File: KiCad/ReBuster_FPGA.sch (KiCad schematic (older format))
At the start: 30 parts, among them U1 10M02SCU169, U2 LM1117-3.3

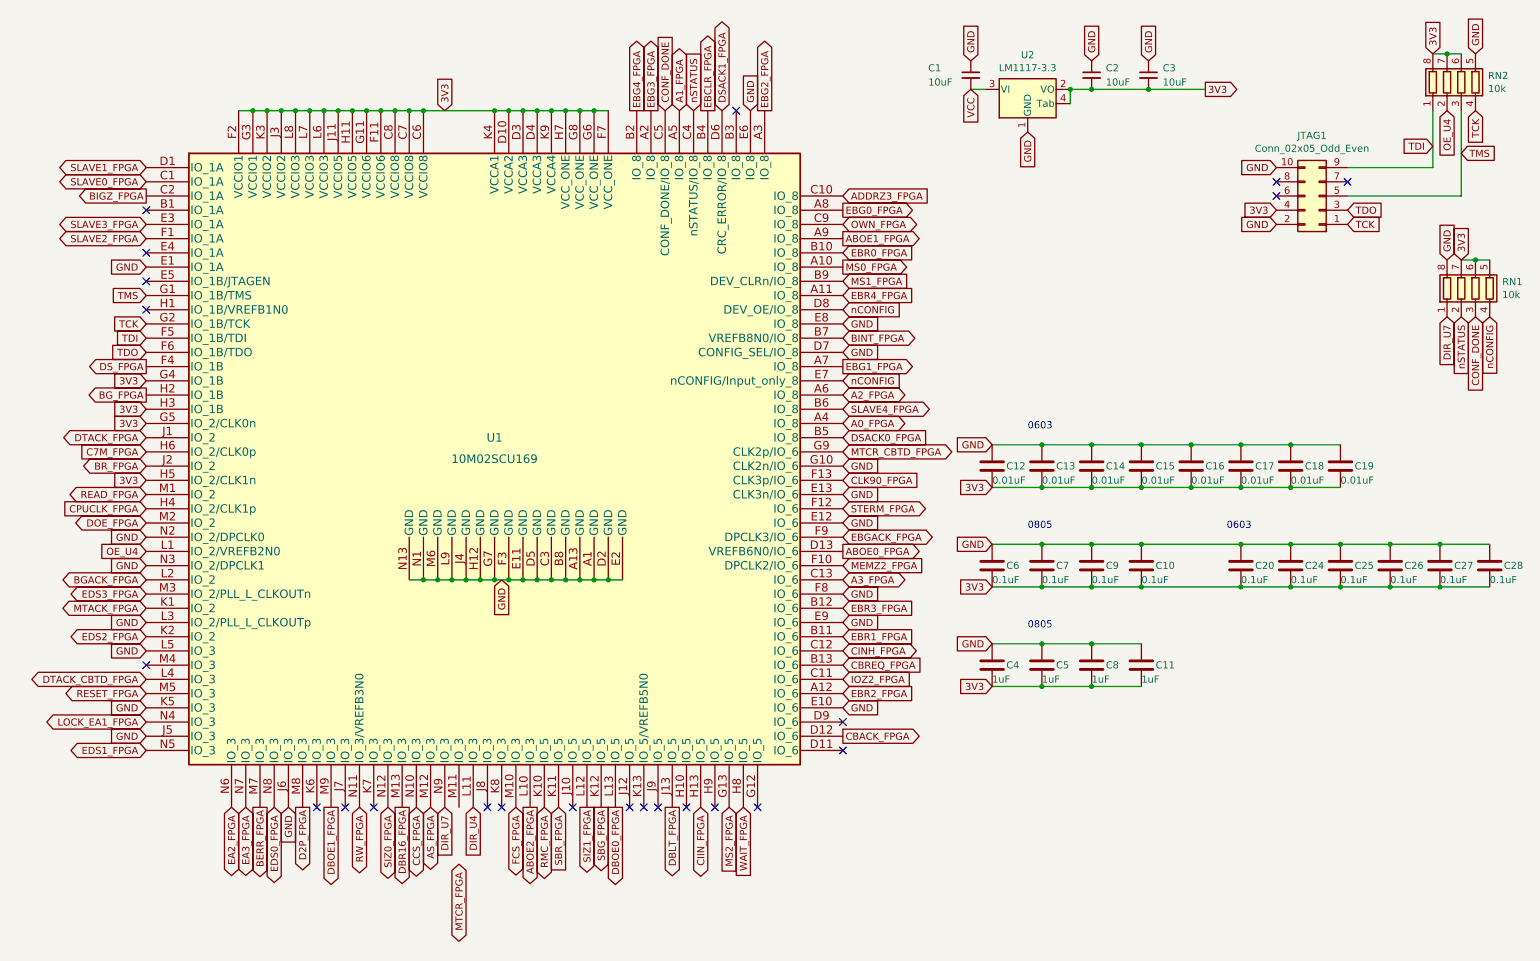
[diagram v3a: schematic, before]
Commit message: Assign MTACK to pin 23,26 in SN74LVC16245 and M11 in FPGA and route trace
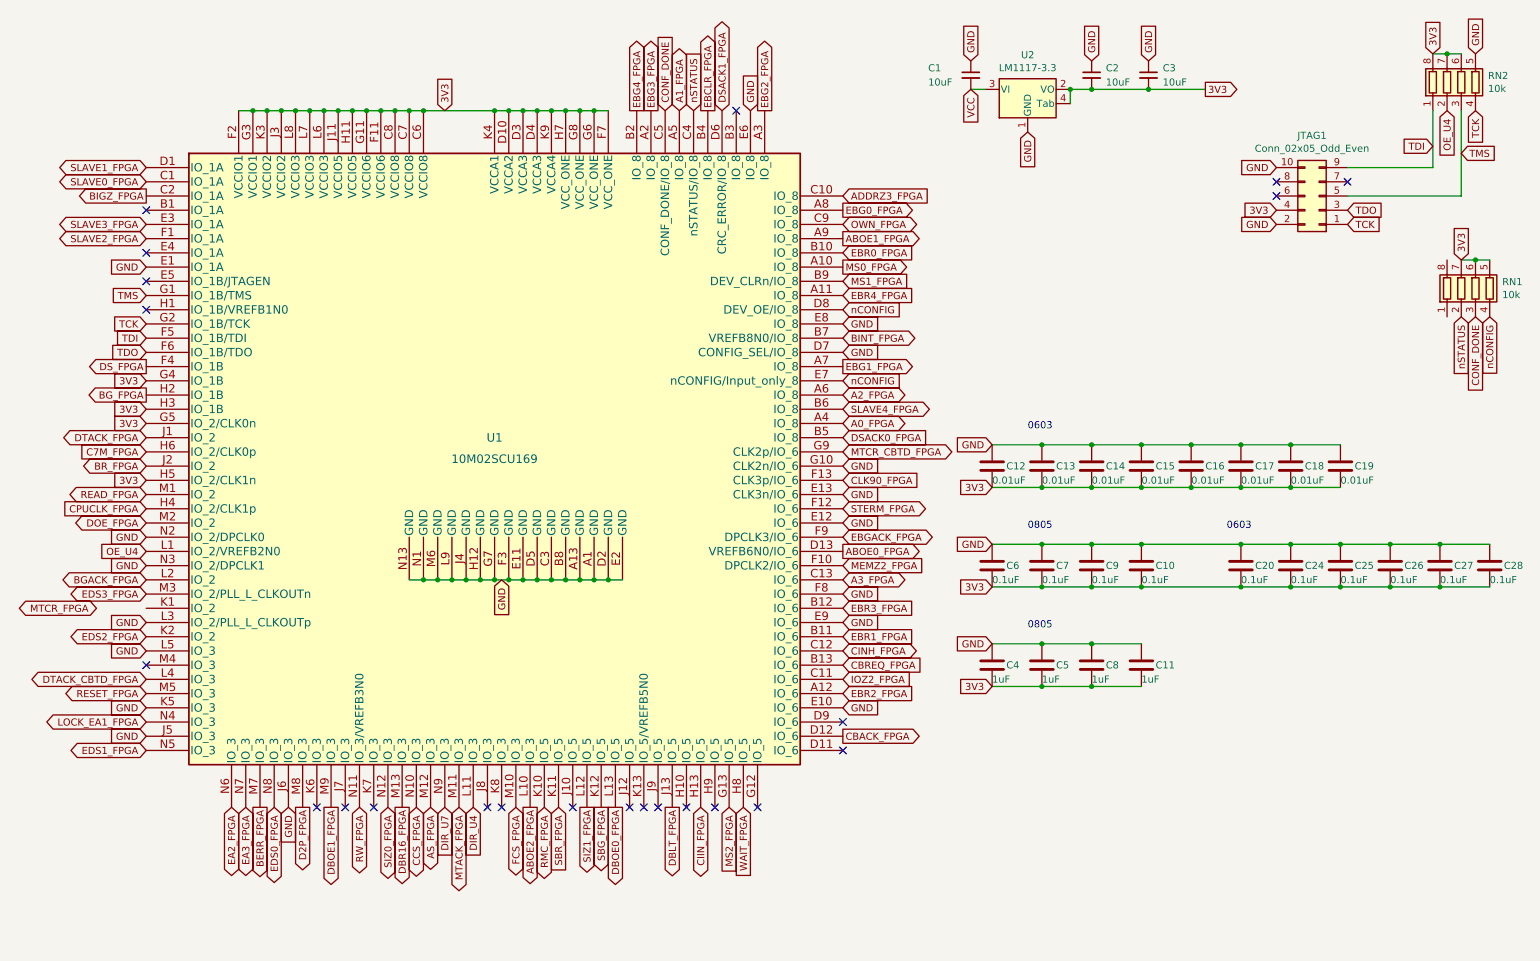
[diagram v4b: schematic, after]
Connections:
- net DIR_U7: no longer RN1.1 (R1.1)
- net GND: no longer RN1.8 (R1.2)
- net MTACK_FPGA: now also U1.M11 (IO_3); no longer U1.K1 (IO_2)
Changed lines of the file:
@@
 Text GLabel 1300 3550 0    50   BiDi ~ 0
 DTACK_FPGA
-Text GLabel 1300 4750 0    50   BiDi ~ 0
+Text GLabel 3500 6150 3    50   BiDi ~ 0
 MTACK_FPGA
 Text GLabel 5200 6150 3    50   BiDi ~ 0
@@
 Text GLabel 5400 6150 3    50   Input ~ 0
 MS2_FPGA
-Text GLabel 3500 6550 3    50   BiDi ~ 0
+Text GLabel 950  4750 0    50   BiDi ~ 0
 MTCR_FPGA
 Text GLabel 6200 5050 2    50   BiDi ~ 0
@@
 OE_U4
 NoConn ~ 9250 1750
-Text GLabel 10450 2700 3    50   Input ~ 0
-DIR_U7
-Text GLabel 10450 2300 1    50   Input ~ 0
-GND
 Text GLabel 3400 6150 3    50   Input ~ 0
 DIR_U7

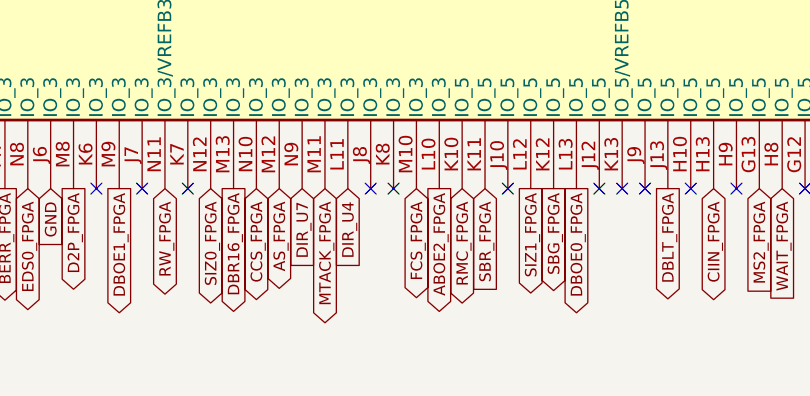
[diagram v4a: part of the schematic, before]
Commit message: Assign SIZ1 to pin 19,30 in SN74LVC16245 and M12 in FPGA and route trace
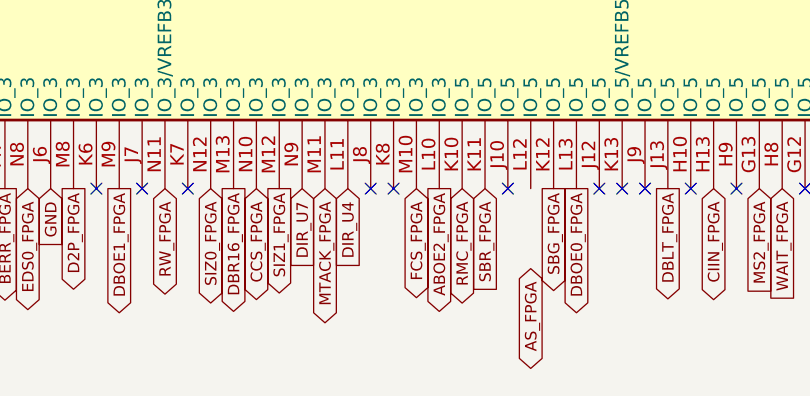
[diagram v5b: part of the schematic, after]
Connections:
- net AS_FPGA: no longer U1.M12 (IO_3)
- net SIZ1_FPGA: now also U1.M12 (IO_3); no longer U1.L12 (IO_5)
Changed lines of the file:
@@
 Text GLabel 1300 3050 0    50   Output ~ 0
 DS_FPGA
-Text GLabel 3300 6150 3    50   BiDi ~ 0
+Text GLabel 4400 6500 3    50   BiDi ~ 0
 AS_FPGA
 Text GLabel 1300 2050 0    50   BiDi ~ 0
@@
 Text GLabel 6200 5150 2    50   Input ~ 0
 CBREQ_FPGA
-Text GLabel 4400 6150 3    50   Output ~ 0
+Text GLabel 3300 6150 3    50   Output ~ 0
 SIZ1_FPGA
 Text GLabel 4600 6150 3    50   Output ~ 0

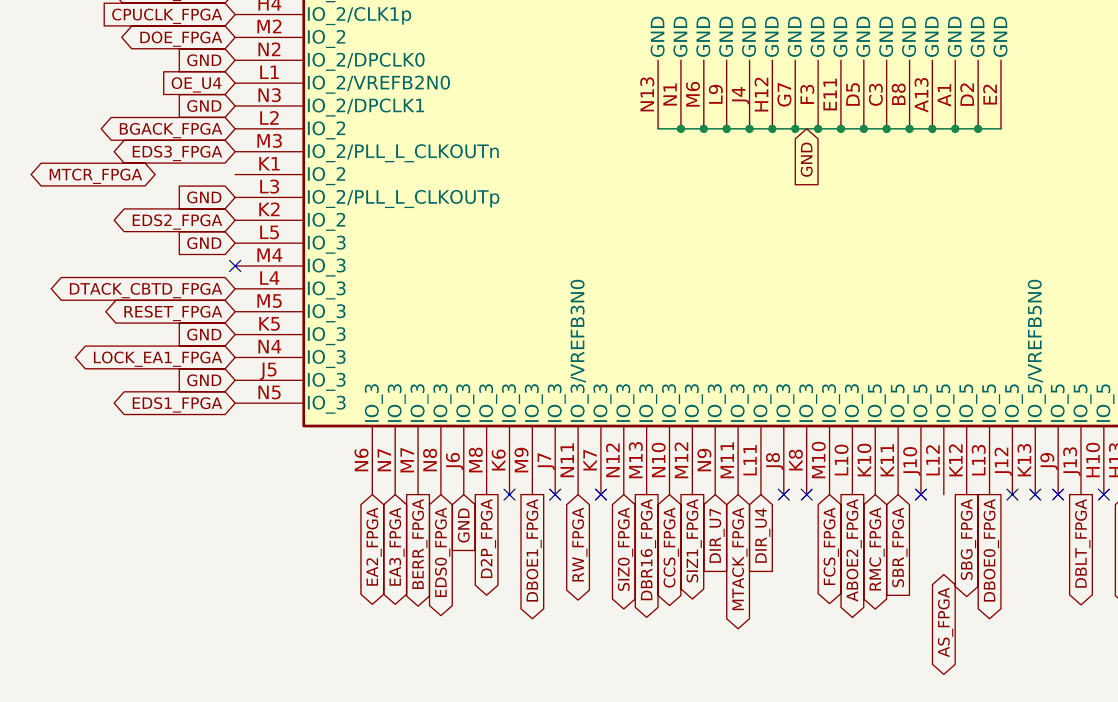
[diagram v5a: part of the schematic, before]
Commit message: Assign AS to pin 17,32 in SN74LVC16245 and L12 in FPGA and route trace
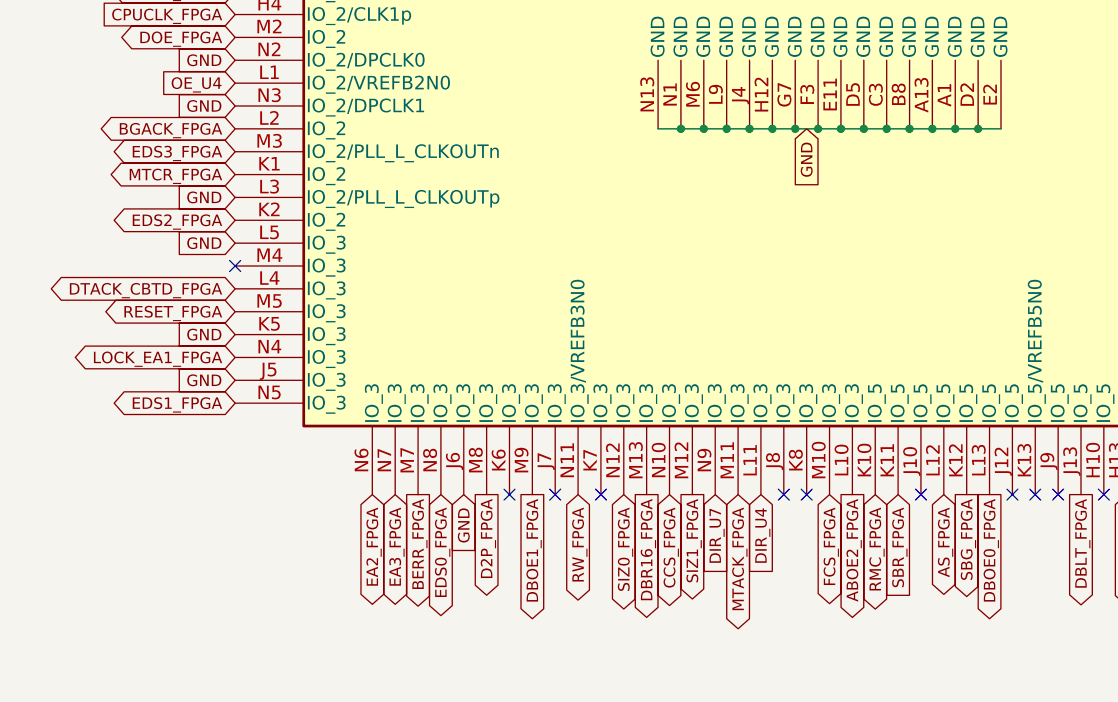
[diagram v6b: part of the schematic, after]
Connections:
- net AS_FPGA: now also U1.L12 (IO_5)
- net MTCR_FPGA: now also U1.K1 (IO_2)
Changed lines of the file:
@@
 Text GLabel 1300 3050 0    50   Output ~ 0
 DS_FPGA
-Text GLabel 4400 6500 3    50   BiDi ~ 0
+Text GLabel 4400 6150 3    50   BiDi ~ 0
 AS_FPGA
 Text GLabel 1300 2050 0    50   BiDi ~ 0
@@
 Text GLabel 5400 6150 3    50   Input ~ 0
 MS2_FPGA
-Text GLabel 950  4750 0    50   BiDi ~ 0
+Text GLabel 1300 4750 0    50   BiDi ~ 0
 MTCR_FPGA
 Text GLabel 6200 5050 2    50   BiDi ~ 0

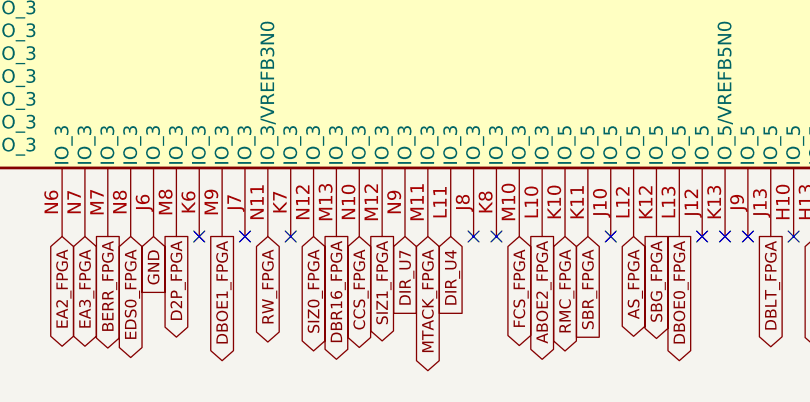
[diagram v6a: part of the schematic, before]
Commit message: Some small power routing improvements and via positioning
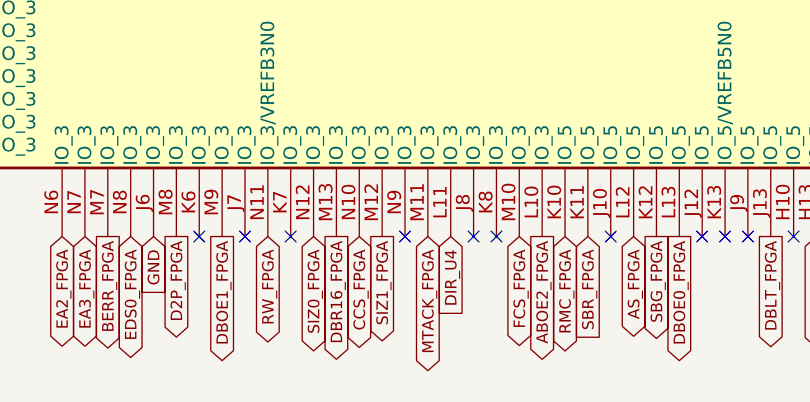
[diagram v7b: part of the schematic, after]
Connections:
- net DIR_U7: no longer names the net of U1.N9 (IO_3)
- no-connect marks 23 -> 24
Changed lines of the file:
@@
 OE_U4
 NoConn ~ 9250 1750
-Text GLabel 3400 6150 3    50   Input ~ 0
-DIR_U7
 Text GLabel 1300 4350 0    50   Input ~ 0
 OE_U4
@@
 Wire Wire Line
 	9000 4600 9350 4600
+NoConn ~ 3400 6150
 $EndSCHEMATC

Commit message: Change C18 from handsolder footprint to normal
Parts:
- C18: footprint Capacitor_SMD:C_0603_1608Metric_Pad1.05x0.95mm_HandSolder -> Capacitor_SMD:C_0603_1608Metric
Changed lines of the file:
@@
 F 0 "C18" H 9450 3750 50  0000 L CNN
 F 1 "0.01uF" H 9350 3650 50  0000 L CNN
-F 2 "Capacitor_SMD:C_0603_1608Metric_Pad1.05x0.95mm_HandSolder" H 9388 3600 50  0001 C CNN
+F 2 "Capacitor_SMD:C_0603_1608Metric" H 9388 3600 50  0001 C CNN
 F 3 "~" H 9350 3750 50  0001 C CNN
 	1    9350 3750
